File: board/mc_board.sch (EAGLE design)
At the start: 15 parts, among them IC1 MEGA8-P, Q1 16MHz

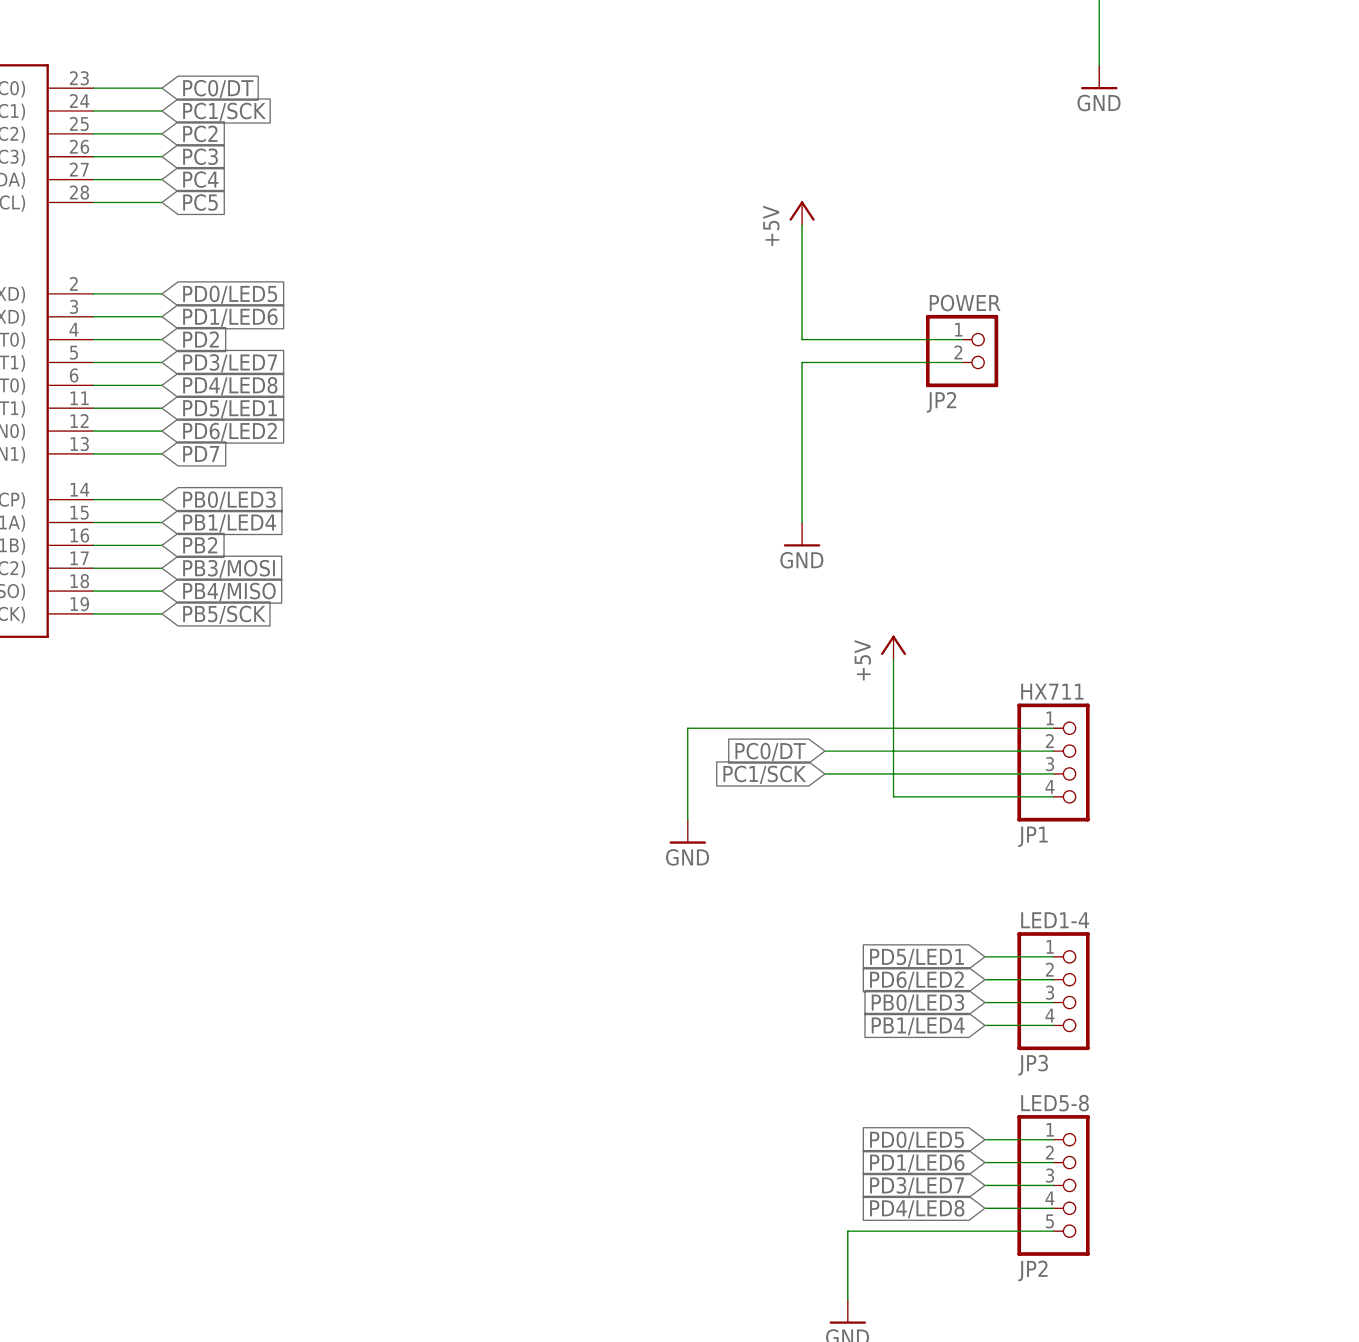
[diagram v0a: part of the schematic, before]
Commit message: added UART pins to layout
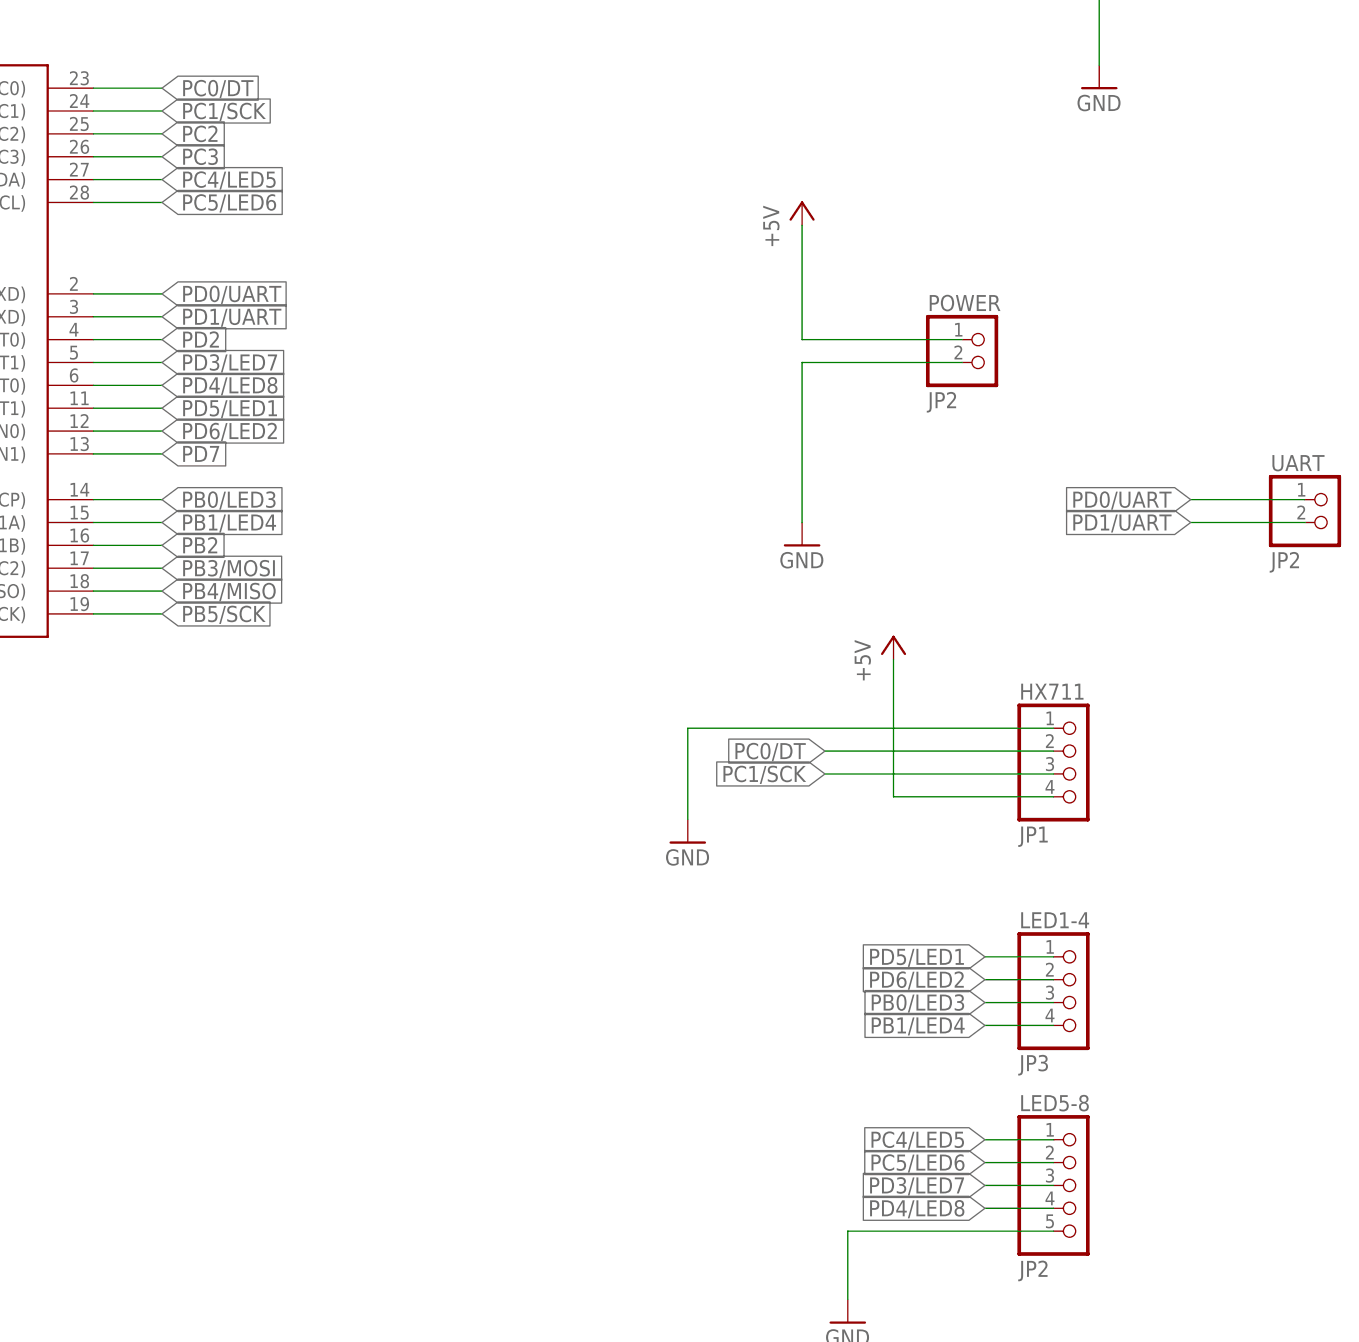
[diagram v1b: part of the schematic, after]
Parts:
- added UART: JP2, pinhead:PINHD-1X2
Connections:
- removed net PC4: IC1.PC4(ADC4/SDA)
- removed net PC5: IC1.PC5(ADC5/SCL)
- removed net PD0/LED5: IC1.PD0(RXD), LED5-8.1
- removed net PD1/LED6: IC1.PD1(TXD), LED5-8.2
- new net PC4/LED5: IC1.PC4(ADC4/SDA), LED5-8.1
- new net PC5/LED6: IC1.PC5(ADC5/SCL), LED5-8.2
- new net PD0/UART: IC1.PD0(RXD), UART.1
- new net PD1/UART: IC1.PD1(TXD), UART.2
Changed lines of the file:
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@@
 <part name="LED1-4" library="pinhead" deviceset="PINHD-1X4" device="" value="JP3"/>
 <part name="GND8" library="supply1" deviceset="GND" device=""/>
+<part name="UART" library="pinhead" deviceset="PINHD-1X2" device="" value="JP2"/>
 </parts>
 <sheets>
@@
 <instance part="LED1-4" gate="A" x="342.9" y="86.36"/>
 <instance part="GND8" gate="1" x="317.5" y="50.8"/>
+<instance part="UART" gate="G$1" x="370.84" y="139.7"/>
 </instances>
 <busses>
@@
 </segment>
 </net>
-<net name="PD1/LED6" class="0">
-<segment>
-<wire x1="241.3" y1="162.56" x2="233.68" y2="162.56" width="0.1524" layer="91"/>
-<pinref part="IC1" gate="G$1" pin="PD1(TXD)"/>
-<label x="241.3" y="162.56" size="1.778" layer="95" xref="yes"/>
+<net name="PD3/LED7" class="0">
+<segment>
+<wire x1="233.68" y1="157.48" x2="241.3" y2="157.48" width="0.1524" layer="91"/>
+<pinref part="IC1" gate="G$1" pin="PD3(INT1)"/>
+<label x="241.3" y="157.48" size="1.778" layer="95" xref="yes"/>
+</segment>
+<segment>
+<wire x1="340.36" y1="66.04" x2="332.74" y2="66.04" width="0.1524" layer="91"/>
+<pinref part="LED5-8" gate="A" pin="3"/>
+<label x="332.74" y="66.04" size="1.778" layer="95" rot="MR0" xref="yes"/>
+</segment>
+</net>
+<net name="PD4/LED8" class="0">
+<segment>
+<wire x1="241.3" y1="154.94" x2="233.68" y2="154.94" width="0.1524" layer="91"/>
+<pinref part="IC1" gate="G$1" pin="PD4(XCK/T0)"/>
+<label x="241.3" y="154.94" size="1.778" layer="95" xref="yes"/>
+</segment>
+<segment>
+<wire x1="340.36" y1="63.5" x2="332.74" y2="63.5" width="0.1524" layer="91"/>
+<pinref part="LED5-8" gate="A" pin="4"/>
+<label x="332.74" y="63.5" size="1.778" layer="95" rot="MR0" xref="yes"/>
+</segment>
+</net>
+<net name="PD7" class="0">
+<segment>
+<wire x1="241.3" y1="147.32" x2="233.68" y2="147.32" width="0.1524" layer="91"/>
+<pinref part="IC1" gate="G$1" pin="PD7(AIN1)"/>
+<label x="241.3" y="147.32" size="1.778" layer="95" xref="yes"/>
+</segment>
+</net>
+<net name="PC0/DT" class="0">
+<segment>
+<wire x1="233.68" y1="187.96" x2="241.3" y2="187.96" width="0.1524" layer="91"/>
+<pinref part="IC1" gate="G$1" pin="PC0(ADC0)"/>
+<label x="241.3" y="187.96" size="1.778" layer="95" xref="yes"/>
+</segment>
+<segment>
+<pinref part="HX711" gate="A" pin="2"/>
+<wire x1="340.36" y1="114.3" x2="314.96" y2="114.3" width="0.1524" layer="91"/>
+<label x="314.96" y="114.3" size="1.778" layer="95" rot="MR0" xref="yes"/>
+</segment>
+</net>
+<net name="PC1/SCK" class="0">
+<segment>
+<wire x1="233.68" y1="185.42" x2="241.3" y2="185.42" width="0.1524" layer="91"/>
+<pinref part="IC1" gate="G$1" pin="PC1(ADC1)"/>
+<label x="241.3" y="185.42" size="1.778" layer="95" xref="yes"/>
+</segment>
+<segment>
+<pinref part="HX711" gate="A" pin="3"/>
+<wire x1="340.36" y1="111.76" x2="314.96" y2="111.76" width="0.1524" layer="91"/>
+<label x="314.96" y="111.76" size="1.778" layer="95" rot="MR0" xref="yes"/>
+</segment>
+</net>
+<net name="PC2" class="0">
+<segment>
+<wire x1="233.68" y1="182.88" x2="241.3" y2="182.88" width="0.1524" layer="91"/>
+<pinref part="IC1" gate="G$1" pin="PC2(ADC2)"/>
+<label x="241.3" y="182.88" size="1.778" layer="95" xref="yes"/>
+</segment>
+</net>
+<net name="PC3" class="0">
+<segment>
+<wire x1="233.68" y1="180.34" x2="241.3" y2="180.34" width="0.1524" layer="91"/>
+<pinref part="IC1" gate="G$1" pin="PC3(ADC3)"/>
+<label x="241.3" y="180.34" size="1.778" layer="95" xref="yes"/>
+</segment>
+</net>
+<net name="PC4/LED5" class="0">
+<segment>
+<wire x1="233.68" y1="177.8" x2="241.3" y2="177.8" width="0.1524" layer="91"/>
+<pinref part="IC1" gate="G$1" pin="PC4(ADC4/SDA)"/>
+<label x="241.3" y="177.8" size="1.778" layer="95" xref="yes"/>
+</segment>
+<segment>
+<wire x1="340.36" y1="71.12" x2="332.74" y2="71.12" width="0.1524" layer="91"/>
+<pinref part="LED5-8" gate="A" pin="1"/>
+<label x="332.74" y="71.12" size="1.778" layer="95" rot="MR0" xref="yes"/>
+</segment>
+</net>
+<net name="PC5/LED6" class="0">
+<segment>
+<wire x1="233.68" y1="175.26" x2="241.3" y2="175.26" width="0.1524" layer="91"/>
+<pinref part="IC1" gate="G$1" pin="PC5(ADC5/SCL)"/>
+<label x="241.3" y="175.26" size="1.778" layer="95" xref="yes"/>
 </segment>
 <segment>
@@
 <pinref part="LED5-8" gate="A" pin="2"/>
 <label x="332.74" y="68.58" size="1.778" layer="95" rot="MR0" xref="yes"/>
-</segment>
-</net>
-<net name="PD3/LED7" class="0">
-<segment>
-<wire x1="233.68" y1="157.48" x2="241.3" y2="157.48" width="0.1524" layer="91"/>
-<pinref part="IC1" gate="G$1" pin="PD3(INT1)"/>
-<label x="241.3" y="157.48" size="1.778" layer="95" xref="yes"/>
-</segment>
-<segment>
-<wire x1="340.36" y1="66.04" x2="332.74" y2="66.04" width="0.1524" layer="91"/>
-<pinref part="LED5-8" gate="A" pin="3"/>
-<label x="332.74" y="66.04" size="1.778" layer="95" rot="MR0" xref="yes"/>
-</segment>
-</net>
-<net name="PD4/LED8" class="0">
-<segment>
-<wire x1="241.3" y1="154.94" x2="233.68" y2="154.94" width="0.1524" layer="91"/>
-<pinref part="IC1" gate="G$1" pin="PD4(XCK/T0)"/>
-<label x="241.3" y="154.94" size="1.778" layer="95" xref="yes"/>
-</segment>
-<segment>
-<wire x1="340.36" y1="63.5" x2="332.74" y2="63.5" width="0.1524" layer="91"/>
-<pinref part="LED5-8" gate="A" pin="4"/>
-<label x="332.74" y="63.5" size="1.778" layer="95" rot="MR0" xref="yes"/>
-</segment>
-</net>
-<net name="PD0/LED5" class="0">
-<segment>
-<wire x1="241.3" y1="165.1" x2="233.68" y2="165.1" width="0.1524" layer="91"/>
-<pinref part="IC1" gate="G$1" pin="PD0(RXD)"/>
-<label x="241.3" y="165.1" size="1.778" layer="95" xref="yes"/>
-</segment>
-<segment>
-<wire x1="340.36" y1="71.12" x2="332.74" y2="71.12" width="0.1524" layer="91"/>
-<pinref part="LED5-8" gate="A" pin="1"/>
-<label x="332.74" y="71.12" size="1.778" layer="95" rot="MR0" xref="yes"/>
-</segment>
-</net>
-<net name="PD7" class="0">
-<segment>
-<wire x1="241.3" y1="147.32" x2="233.68" y2="147.32" width="0.1524" layer="91"/>
-<pinref part="IC1" gate="G$1" pin="PD7(AIN1)"/>
-<label x="241.3" y="147.32" size="1.778" layer="95" xref="yes"/>
-</segment>
-</net>
-<net name="PC0/DT" class="0">
-<segment>
-<wire x1="233.68" y1="187.96" x2="241.3" y2="187.96" width="0.1524" layer="91"/>
-<pinref part="IC1" gate="G$1" pin="PC0(ADC0)"/>
-<label x="241.3" y="187.96" size="1.778" layer="95" xref="yes"/>
-</segment>
-<segment>
-<pinref part="HX711" gate="A" pin="2"/>
-<wire x1="340.36" y1="114.3" x2="314.96" y2="114.3" width="0.1524" layer="91"/>
-<label x="314.96" y="114.3" size="1.778" layer="95" rot="MR0" xref="yes"/>
-</segment>
-</net>
-<net name="PC1/SCK" class="0">
-<segment>
-<wire x1="233.68" y1="185.42" x2="241.3" y2="185.42" width="0.1524" layer="91"/>
-<pinref part="IC1" gate="G$1" pin="PC1(ADC1)"/>
-<label x="241.3" y="185.42" size="1.778" layer="95" xref="yes"/>
-</segment>
-<segment>
-<pinref part="HX711" gate="A" pin="3"/>
-<wire x1="340.36" y1="111.76" x2="314.96" y2="111.76" width="0.1524" layer="91"/>
-<label x="314.96" y="111.76" size="1.778" layer="95" rot="MR0" xref="yes"/>
-</segment>
-</net>
-<net name="PC2" class="0">
-<segment>
-<wire x1="233.68" y1="182.88" x2="241.3" y2="182.88" width="0.1524" layer="91"/>
-<pinref part="IC1" gate="G$1" pin="PC2(ADC2)"/>
-<label x="241.3" y="182.88" size="1.778" layer="95" xref="yes"/>
-</segment>
-</net>
-<net name="PC3" class="0">
-<segment>
-<wire x1="233.68" y1="180.34" x2="241.3" y2="180.34" width="0.1524" layer="91"/>
-<pinref part="IC1" gate="G$1" pin="PC3(ADC3)"/>
-<label x="241.3" y="180.34" size="1.778" layer="95" xref="yes"/>
-</segment>
-</net>
-<net name="PC4" class="0">
-<segment>
-<wire x1="233.68" y1="177.8" x2="241.3" y2="177.8" width="0.1524" layer="91"/>
-<pinref part="IC1" gate="G$1" pin="PC4(ADC4/SDA)"/>
-<label x="241.3" y="177.8" size="1.778" layer="95" xref="yes"/>
-</segment>
-</net>
-<net name="PC5" class="0">
-<segment>
-<wire x1="233.68" y1="175.26" x2="241.3" y2="175.26" width="0.1524" layer="91"/>
-<pinref part="IC1" gate="G$1" pin="PC5(ADC5/SCL)"/>
-<label x="241.3" y="175.26" size="1.778" layer="95" xref="yes"/>
 </segment>
 </net>
@@
 </segment>
 </net>
+<net name="PD0/UART" class="0">
+<segment>
+<wire x1="241.3" y1="165.1" x2="233.68" y2="165.1" width="0.1524" layer="91"/>
+<pinref part="IC1" gate="G$1" pin="PD0(RXD)"/>
+<label x="241.3" y="165.1" size="1.778" layer="95" xref="yes"/>
+</segment>
+<segment>
+<pinref part="UART" gate="G$1" pin="1"/>
+<wire x1="368.3" y1="142.24" x2="355.6" y2="142.24" width="0.1524" layer="91"/>
+<label x="355.6" y="142.24" size="1.778" layer="95" rot="MR0" xref="yes"/>
+</segment>
+</net>
+<net name="PD1/UART" class="0">
+<segment>
+<wire x1="241.3" y1="162.56" x2="233.68" y2="162.56" width="0.1524" layer="91"/>
+<pinref part="IC1" gate="G$1" pin="PD1(TXD)"/>
+<label x="241.3" y="162.56" size="1.778" layer="95" xref="yes"/>
+</segment>
+<segment>
+<pinref part="UART" gate="G$1" pin="2"/>
+<wire x1="368.3" y1="139.7" x2="355.6" y2="139.7" width="0.1524" layer="91"/>
+<label x="355.6" y="139.7" size="1.778" layer="95" rot="MR0" xref="yes"/>
+</segment>
+</net>
